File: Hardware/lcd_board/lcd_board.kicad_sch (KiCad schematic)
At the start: 13 parts, among them J1 Conn_01x40, J2 Conn_01x16, U1 74HC04, U2 74HC173, U3 74HC173, U4 74HC173

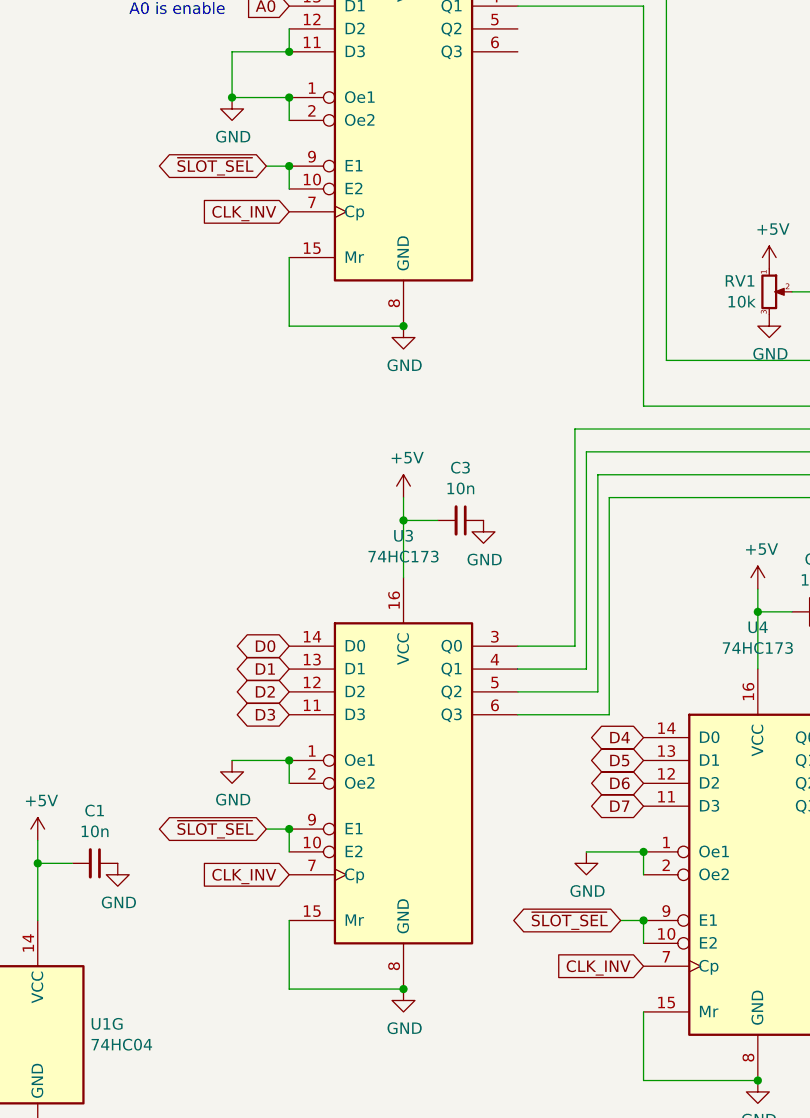
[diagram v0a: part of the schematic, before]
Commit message: Add R/W to LCD board enable
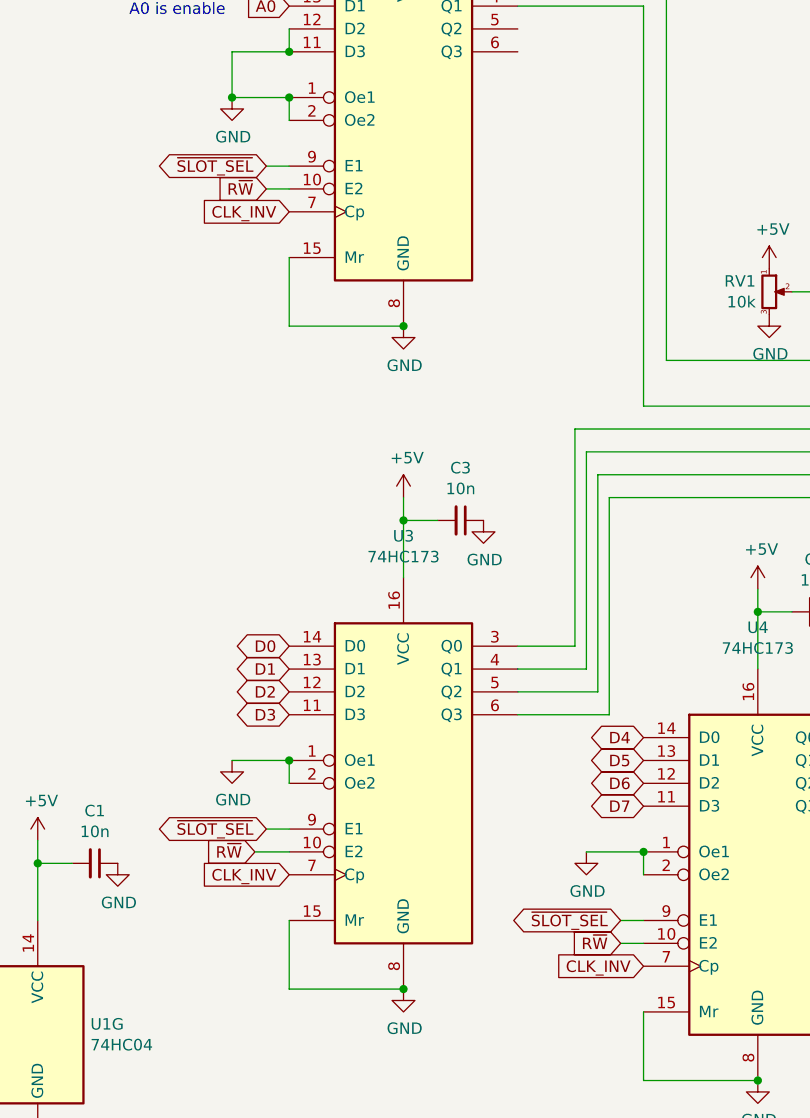
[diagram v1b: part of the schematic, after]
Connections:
- net R~{W}: now also U2.10 (E2), U3.10 (E2), U4.10 (E2)
- net ~{SLOT_SEL}: no longer U2.10 (E2), U3.10 (E2), U4.10 (E2)
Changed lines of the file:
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@@
   (junction (at 154.94 147.32) (diameter 0) (color 0 0 0 0)
   )
-  (junction (at 181.61 139.7) (diameter 0) (color 0 0 0 0)
-  )
   (junction (at 31.75 83.82) (diameter 0) (color 0 0 0 0)
   )
@@
   (junction (at 207.01 54.61) (diameter 0) (color 0 0 0 0)
   )
-  (junction (at 142.24 55.88) (diameter 0) (color 0 0 0 0)
-  )
   (junction (at 135.89 48.26) (diameter 0) (color 0 0 0 0)
   )
@@
   (junction (at 49.53 165.1) (diameter 0) (color 0 0 0 0)
   )
-  (junction (at 142.24 129.54) (diameter 0) (color 0 0 0 0)
-  )
   (junction (at 35.56 91.44) (diameter 0) (color 0 0 0 0)
   )
@@
     (stroke (width 0) (type default) (color 0 0 0 0))
   )
-  (wire (pts (xy 142.24 58.42) (xy 142.24 55.88))
-    (stroke (width 0) (type default) (color 0 0 0 0))
-  )
   (wire (pts (xy 218.44 82.55) (xy 181.61 82.55))
     (stroke (width 0) (type default) (color 0 0 0 0))
@@
     (stroke (width 0) (type default) (color 0 0 0 0))
   )
+  (wire (pts (xy 138.43 132.08) (xy 142.24 132.08))
+    (stroke (width 0) (type default) (color 0 0 0 0))
+  )
   (wire (pts (xy 212.09 121.92) (xy 212.09 97.79))
     (stroke (width 0) (type default) (color 0 0 0 0))
@@
     (stroke (width 0) (type default) (color 0 0 0 0))
   )
+  (wire (pts (xy 179.07 142.24) (xy 181.61 142.24))
+    (stroke (width 0) (type default) (color 0 0 0 0))
+  )
   (wire (pts (xy 118.11 133.35) (xy 114.3 133.35))
     (stroke (width 0) (type default) (color 0 0 0 0))
@@
     (stroke (width 0) (type default) (color 0 0 0 0))
   )
-  (wire (pts (xy 181.61 142.24) (xy 181.61 139.7))
-    (stroke (width 0) (type default) (color 0 0 0 0))
-  )
   (wire (pts (xy 44.45 87.63) (xy 49.53 87.63))
     (stroke (width 0) (type default) (color 0 0 0 0))
@@
     (stroke (width 0) (type default) (color 0 0 0 0))
   )
-  (wire (pts (xy 142.24 132.08) (xy 142.24 129.54))
-    (stroke (width 0) (type default) (color 0 0 0 0))
-  )
   (wire (pts (xy 33.02 86.36) (xy 33.02 83.82))
+    (stroke (width 0) (type default) (color 0 0 0 0))
+  )
+  (wire (pts (xy 139.7 58.42) (xy 142.24 58.42))
     (stroke (width 0) (type default) (color 0 0 0 0))
   )
@@
     )
   )
+  (global_label "R~{W}" (shape input) (at 179.07 142.24 180) (fields_autoplaced)
+    (effects (font (size 1.27 1.27)) (justify right))
+    (property "Intersheet References" "${INTERSHEET_REFS}" (id 0) (at 135.89 30.48 0)
+      (effects (font (size 1.27 1.27)) hide)
+    )
+  )
   (global_label "~{SSEL}" (shape bidirectional) (at 62.23 92.71 0) (fields_autoplaced)
     (effects (font (size 1.27 1.27)) (justify left))
@@
     )
   )
+  (global_label "R~{W}" (shape input) (at 139.7 58.42 180) (fields_autoplaced)
+    (effects (font (size 1.27 1.27)) (justify right))
+    (property "Intersheet References" "${INTERSHEET_REFS}" (id 0) (at 96.52 -53.34 0)
+      (effects (font (size 1.27 1.27)) hide)
+    )
+  )
   (global_label "RDY" (shape input) (at 49.53 105.41 180) (fields_autoplaced)
     (effects (font (size 1.27 1.27)) (justify right))
@@
       (effects (font (size 1.27 1.27)) hide)
     )
+  )
+  (global_label "R~{W}" (shape input) (at 138.43 132.08 180) (fields_autoplaced)
+    (effects (font (size 1.27 1.27)) (justify right))
+    (property "Intersheet References" "${INTERSHEET_REFS}" (id 0) (at 95.25 20.32 0)
+      (effects (font (size 1.27 1.27)) hide)
+    )
